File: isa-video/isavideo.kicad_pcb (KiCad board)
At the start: 4 copper layers, 106.4 x 95 mm, 143 parts, among them J1 PROG, J2 DB15_Female_HighDensity_Mount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, J3 PJRAN1X1U04X, J4 10029449-111RLF, J5 Conn_ISA_8bit, J6 RFMOD, J7 Conn_01x05, J8 Conn_02x06_Odd_Even, SW1 SW_DIP_x04, U1 ICE40HX4K-TQ144, U10 APX803S00-29SA-7, U11 74HCT125, U12 TFP410PAP, U2 SST26VF080A-104I/SN, U3 74ALVC164245, U4 74ALVC164245, U5 74ALVC164245, U6 ADA4891-3, U7 IS61WV5128BLL-10KLI, U8 LD1085D2T33R, U9 AP2114HA-1.2, X1 10MHz, X2 14.318MHz

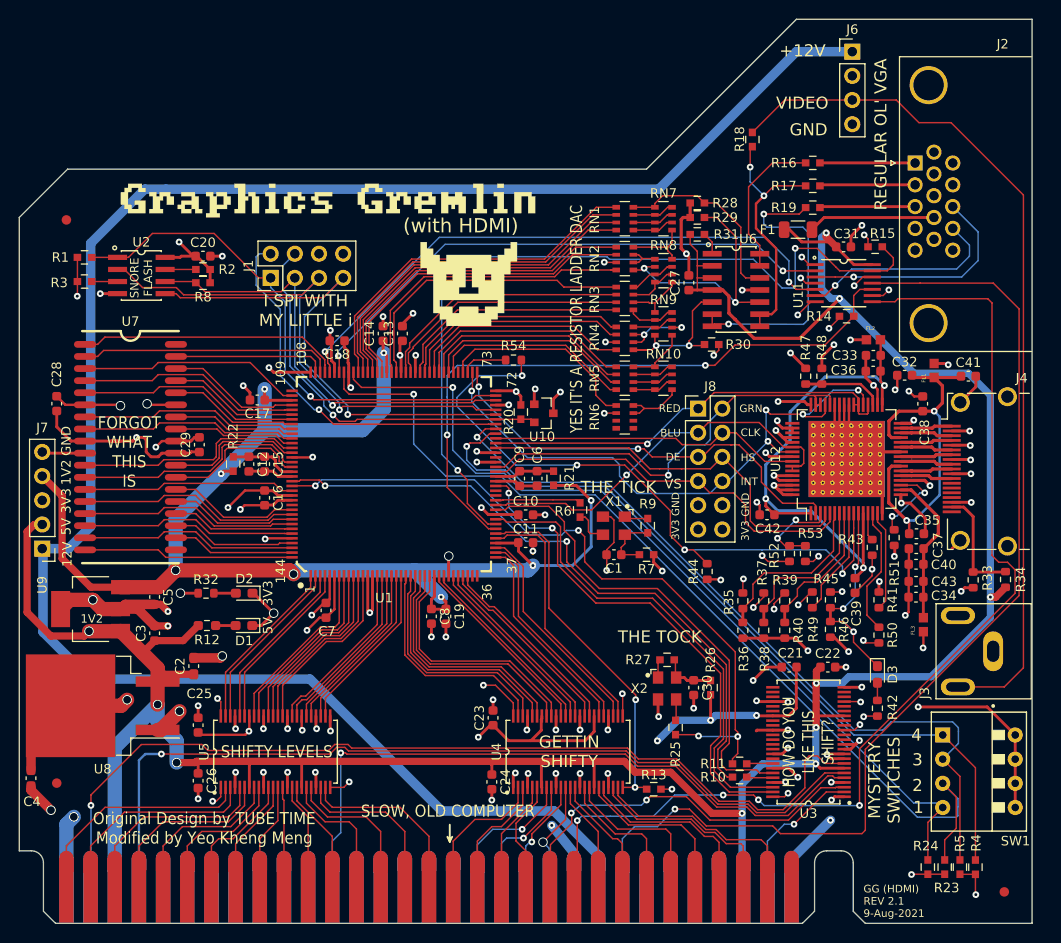
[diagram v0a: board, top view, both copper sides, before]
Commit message: Display CGA colour 6 brown in HDMI port  (#2)
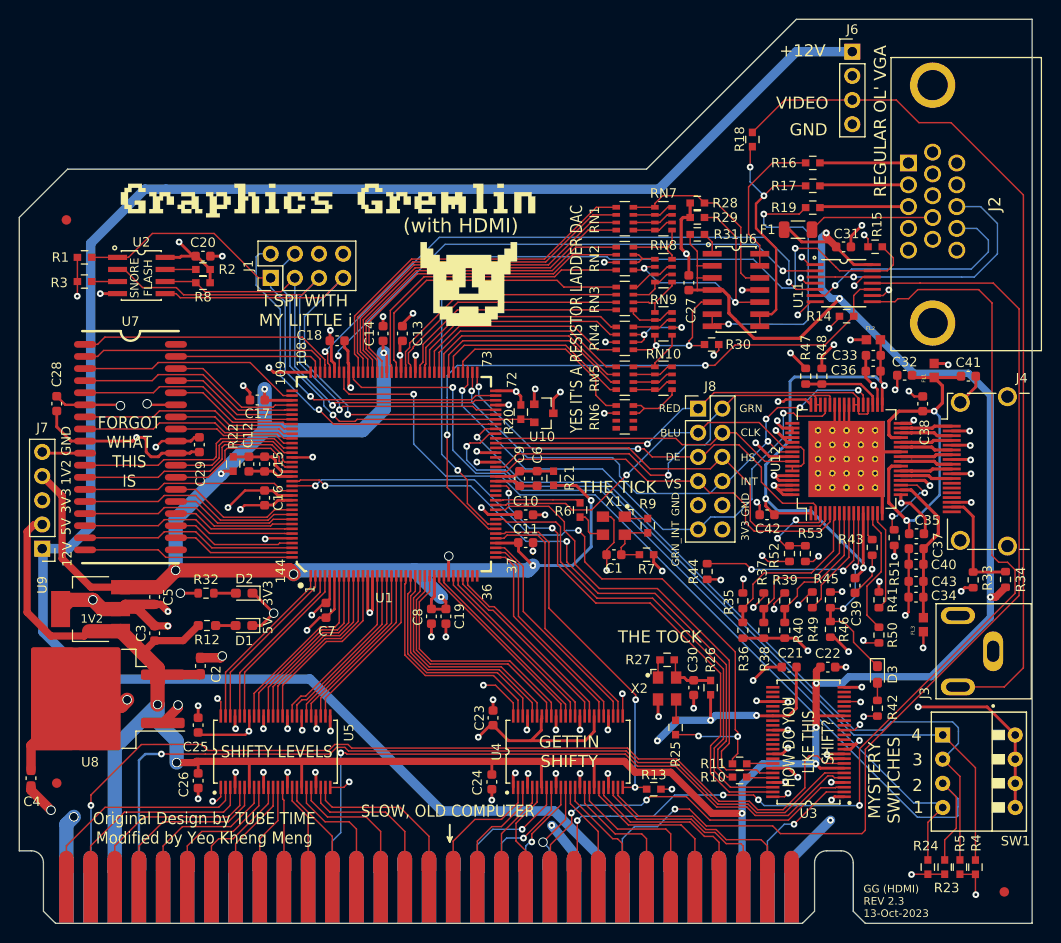
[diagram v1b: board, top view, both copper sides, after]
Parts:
- removed R54: 0, Resistor_SMD:R_0603_1608Metric
- J2: footprint Connector_Dsub:DSUB-15-HD_Female_Horizontal_P2.29x1.98mm_EdgePinOffset8.35mm_Housed_MountingHolesOffset10.89mm -> libraries:23117631
- U12: footprint Package_QFP:HTQFP-64-1EP_10x10mm_P0.5mm_EP8x8mm_Mask4.4x4.4mm_ThermalVias -> libraries:TFP410_ThermalVias
- moved U8 1.52 mm to (99.0, 112.3)
- moved C2 0.70 mm to (110.6, 108.8)
- moved J2 0.70 mm to (185.0, 56.0)
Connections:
- net /Bus Interface/~0WS renamed /Bus Interface/~{0WS}
- net /Bus Interface/~0WS_5V renamed /Bus Interface/~{0WS_5V}
- net /Bus Interface/~IOR_5V renamed /Bus Interface/~{IOR_5V}
- net /Bus Interface/~IOW_5V renamed /Bus Interface/~{IOW_5V}
- net /Bus Interface/~SMEMR_5V renamed /Bus Interface/~{SMEMR_5V}
- net /Bus Interface/~SMEMW_5V renamed /Bus Interface/~{SMEMW_5V}
- net /RAM/~RAM_WE renamed /RAM/~{RAM_WE}
- net /SPI_~CS renamed /SPI_~{CS}
- net /hdmi/PD renamed Net-(U12-~{PD})
- net /~CRESET renamed /~{CRESET}
- net /~IOR renamed /~{IOR}
- net /~IOW renamed /~{IOW}
- net /~SMEMR renamed /~{SMEMR}
- net /~SMEMW renamed /~{SMEMW}
- J2 pad 11: (no net) -> unconnected-(J2-Pad11)
- J2 pad 12: (no net) -> unconnected-(J2-Pad12)
- J2 pad 15: (no net) -> unconnected-(J2-Pad15)
- J2 pad 4: (no net) -> unconnected-(J2-Pad4)
- J3 pad 3: (no net) -> unconnected-(J3-Pad3)
- J4 pad 13: (no net) -> unconnected-(J4-CEC-Pad13)
- J4 pad 14: (no net) -> unconnected-(J4-UTILITY/HEAC+-Pad14)
- J4 pad 15: (no net) -> unconnected-(J4-SCL-Pad15)
- J4 pad 16: (no net) -> unconnected-(J4-SDA-Pad16)
- J4 pad 19: (no net) -> unconnected-(J4-HPD/HEAC--Pad19)
- J5 pad A1: (no net) -> unconnected-(J5-~{IO_CHCK}-PadA1)
- J5 pad B15: (no net) -> unconnected-(J5-~{DACK3}-PadB15)
- J5 pad B16: (no net) -> unconnected-(J5-DRQ3-PadB16)
- J5 pad B17: (no net) -> unconnected-(J5-~{DACK1}-PadB17)
- J5 pad B18: (no net) -> unconnected-(J5-DRQ1-PadB18)
- J5 pad B19: (no net) -> unconnected-(J5-~{REFRESH}-PadB19)
- J5 pad B21: (no net) -> unconnected-(J5-IRQ7-PadB21)
- J5 pad B22: (no net) -> unconnected-(J5-IRQ6-PadB22)
- J5 pad B23: (no net) -> unconnected-(J5-IRQ5-PadB23)
- J5 pad B24: (no net) -> unconnected-(J5-IRQ4-PadB24)
- J5 pad B25: (no net) -> unconnected-(J5-IRQ3-PadB25)
- J5 pad B26: (no net) -> unconnected-(J5-~{DACK2}-PadB26)
- J5 pad B27: (no net) -> unconnected-(J5-TC-PadB27)
- J5 pad B4: (no net) -> unconnected-(J5-IRQ2/9-PadB4)
- J5 pad B5: (no net) -> unconnected-(J5--5V-PadB5)
- J5 pad B6: (no net) -> unconnected-(J5-DRQ2-PadB6)
- J5 pad B7: (no net) -> unconnected-(J5--12V-PadB7)
- J6 pad 2: (no net) -> unconnected-(J6-Pin_2-Pad2)
- J8 pad 11: +3V3 -> /HDMI_GRN_INT
- RN6 pad 3: (no net) -> unconnected-(RN6-R3.1-Pad3)
- RN6 pad 4: (no net) -> unconnected-(RN6-R4.1-Pad4)
- RN6 pad 5: (no net) -> unconnected-(RN6-R4.2-Pad5)
- RN6 pad 6: (no net) -> unconnected-(RN6-R3.2-Pad6)
- U1 pad 109: (no net) -> unconnected-(U1E-VPP_FAST-Pad109)
- U1 pad 133: (no net) -> unconnected-(U1E-NC-Pad133)
- U1 pad 35: (no net) -> unconnected-(U1E-NC-Pad35)
- U1 pad 36: (no net) -> unconnected-(U1E-NC-Pad36)
- U1 pad 50: (no net) -> unconnected-(U1E-NC-Pad50)
- U1 pad 51: (no net) -> unconnected-(U1E-NC-Pad51)
- U1 pad 58: (no net) -> unconnected-(U1E-NC-Pad58)
- U1 pad 75: /HDMI_PD -> /HDMI_GRN_INT
- U1 pad 77: (no net) -> unconnected-(U1E-NC-Pad77)
- U12 pad 45: /HDMI_INT -> /HDMI_GRN_INT
- U12 pad 49: (no net) -> unconnected-(U12-NC-Pad49)
- U3 pad 13: (no net) -> unconnected-(U3-2B0-Pad13)
- U3 pad 14: (no net) -> unconnected-(U3-2B1-Pad14)
- U3 pad 16: (no net) -> unconnected-(U3-2B2-Pad16)
- U3 pad 17: (no net) -> unconnected-(U3-2B3-Pad17)
- U3 pad 19: (no net) -> unconnected-(U3-2B4-Pad19)
- U3 pad 20: (no net) -> unconnected-(U3-2B5-Pad20)
- U3 pad 22: (no net) -> unconnected-(U3-2B6-Pad22)
- U3 pad 23: (no net) -> unconnected-(U3-2B7-Pad23)
- U3 pad 25: (no net) -> unconnected-(U3-2~{OE}-Pad25)
- U3 pad 26: (no net) -> unconnected-(U3-2A7-Pad26)
- U3 pad 27: (no net) -> unconnected-(U3-2A6-Pad27)
- U3 pad 29: (no net) -> unconnected-(U3-2A5-Pad29)
- U3 pad 30: (no net) -> unconnected-(U3-2A4-Pad30)
- U3 pad 32: (no net) -> unconnected-(U3-2A3-Pad32)
- U3 pad 33: (no net) -> unconnected-(U3-2A2-Pad33)
- U3 pad 35: (no net) -> unconnected-(U3-2A1-Pad35)
- U3 pad 36: (no net) -> unconnected-(U3-2A0-Pad36)
- U3 pad 37: (no net) -> unconnected-(U3-1A7-Pad37)
- U3 pad 38: (no net) -> unconnected-(U3-1A6-Pad38)
- U3 pad 40: (no net) -> unconnected-(U3-1A5-Pad40)
- U7 pad 19: (no net) -> unconnected-(U7-NC-Pad19)
- U7 pad 36: (no net) -> unconnected-(U7-NC-Pad36)
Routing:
- net /HDMI_GRN_INT: track 0.00 -> 57.5 mm, vias 0 -> 2
- net Net-(U12-~{PD}): track 70.1 -> 21.1 mm, vias 4 -> 2
- net GND: track 378.1 -> 368.3 mm
- net /HDMI_PD: track 4.90 -> 0.00 mm
- net /HDMI_INT: track 64.0 -> 59.6 mm
- net /VGA_HSYNC_5V: track 24.6 -> 27.7 mm
- net /VGA_VSYNC_5V: track 21.6 -> 24.5 mm
- net /hdmi/DVDD: track 56.1 -> 58.0 mm
- net /hdmi/MSEN: track 22.8 -> 21.0 mm, vias 3 -> 2
- net Net-(RN4-R4.2): track 16.6 -> 15.1 mm
- net +3V3: track 201.0 -> 199.9 mm
- net /Bus Interface/RDY_5V: track 112.8 -> 113.5 mm
- net /B5: track 24.2 -> 23.4 mm
- net /B4: track 23.9 -> 23.2 mm
- net +5V: track 299.5 -> 300.2 mm, vias 10 -> 9
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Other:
- net class Default removed
- board text added: "GG (HDMI) REV 2.3 13-Oct-2023"
- board text added: "GRN_INT"
- board text added: "~{CRESET}"
- board text added: "~{CS}"
- board text removed: "GG (HDMI) REV 2.1 9-Aug-2021"
- board text removed: "~CRESET"
- board text removed: "~CS"

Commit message: V2.4 changes (#3)
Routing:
- net /Bus Interface/~{IOW_5V}: track 24.5 -> 14.1 mm
- net /HDMI_GRN_INT: track 57.5 -> 56.9 mm
- net +5V: track 300.2 -> 299.6 mm
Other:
- board text added: "GG (HDMI) REV 2.4 04-Jan-2024"
- board text removed: "GG (HDMI) REV 2.3 13-Oct-2023"
